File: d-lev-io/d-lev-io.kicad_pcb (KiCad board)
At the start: 2 copper layers, 92 parts, among them J1 USB_C_Receptacle_USB2.0, J2 PJ-059A, J3 Conn_01x12_MountingPin, J4 MIDI_OUT_JACK, J5 PROG_HDR, SW1 SW_Push, SW2 SW_Push, SW3 SW_Push, U1 ATSAMD11D14A-M, U2 TPS54202DDC, U4 MIC5219-3.3YM5, U6 74AHC1G126

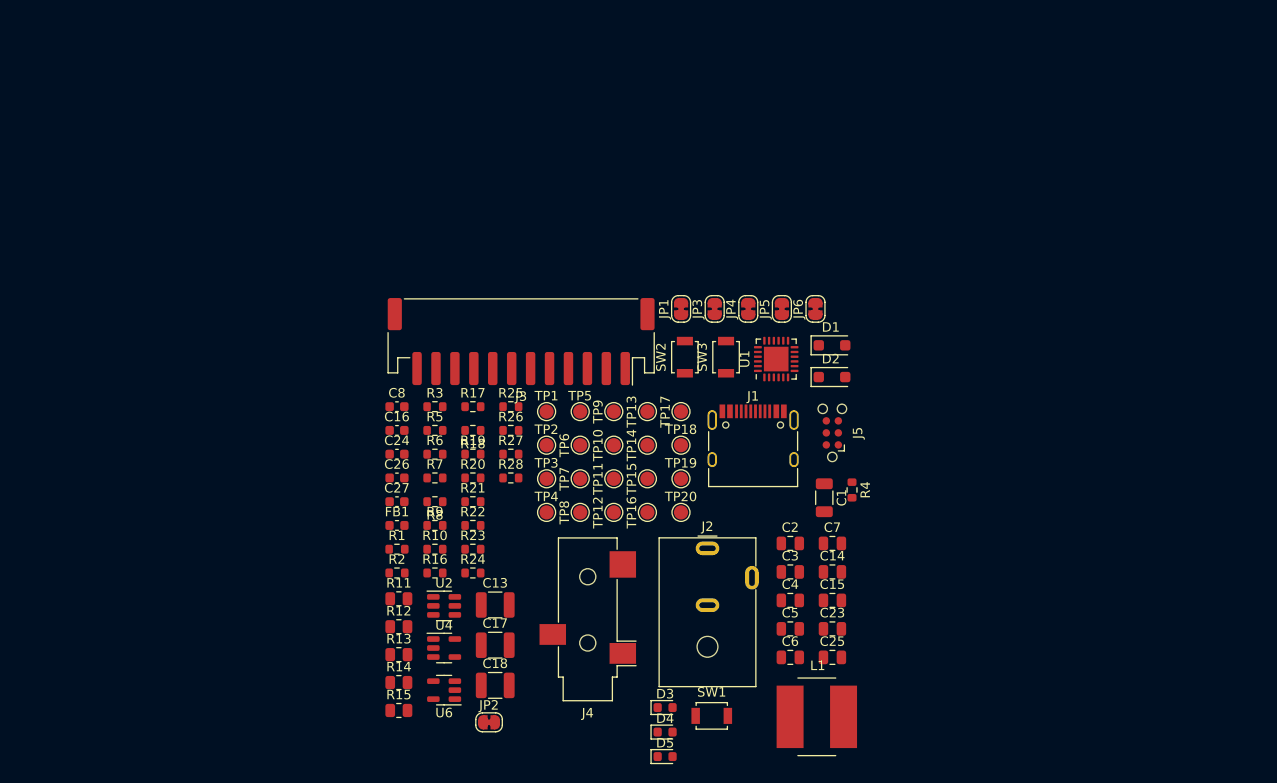
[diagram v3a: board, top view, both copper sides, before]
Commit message: Added DAC schematic to I/O board
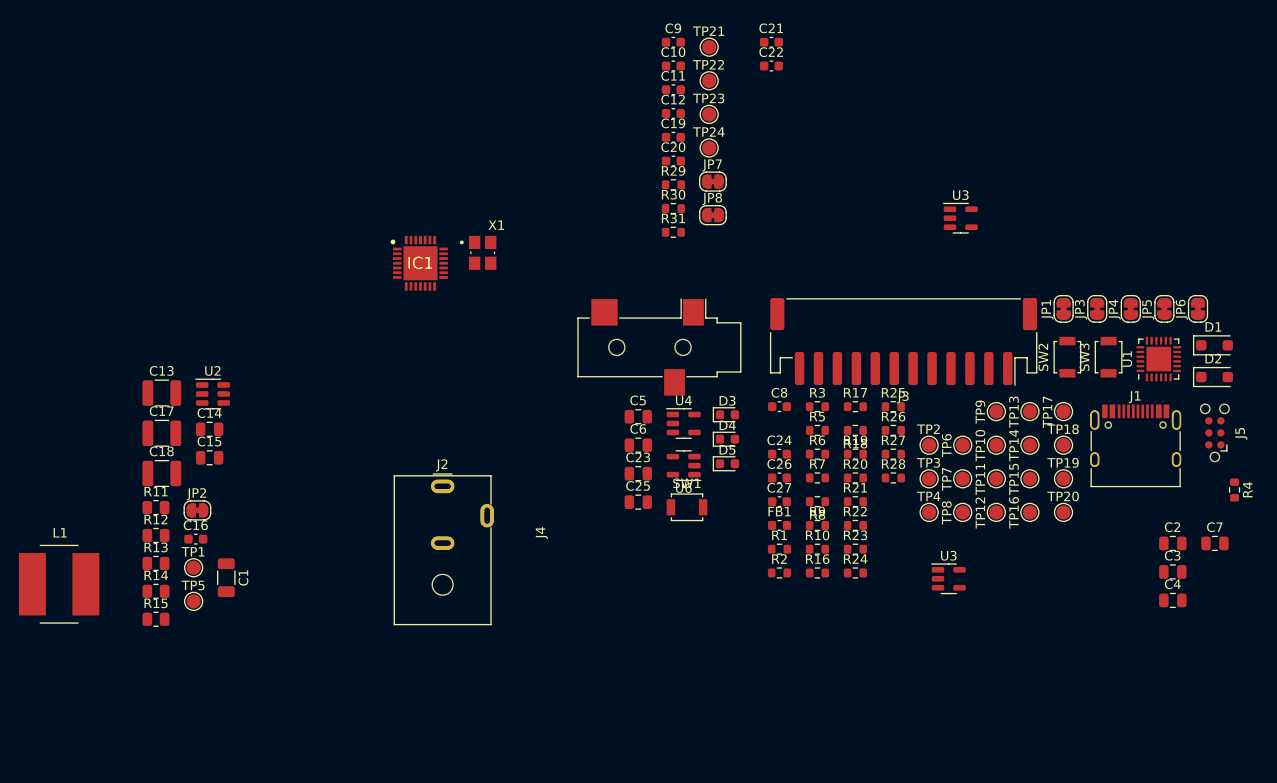
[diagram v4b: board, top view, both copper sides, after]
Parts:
- added C10: 33p, Capacitor_SMD:C_0603_1608Metric, F.Cu at (120.9, 64.2)
- added C11: 1u, Capacitor_SMD:C_0603_1608Metric, F.Cu at (120.9, 66.8)
- added C12: 4.7u, Capacitor_SMD:C_0603_1608Metric, F.Cu at (120.9, 69.3)
- added C19: 1u, Capacitor_SMD:C_0603_1608Metric, F.Cu at (120.9, 71.8)
- added C20: 1u, Capacitor_SMD:C_0603_1608Metric, F.Cu at (120.9, 74.3)
- added C21: 1u, Capacitor_SMD:C_0603_1608Metric, F.Cu at (131.3, 61.7)
- added C22: 1u, Capacitor_SMD:C_0603_1608Metric, F.Cu at (131.3, 64.2)
- added C9: 33p, Capacitor_SMD:C_0603_1608Metric, F.Cu at (120.9, 61.7)
- added IC1: ES9010K2M, ess-dac:QFN50P500X500X90-29N-D, F.Cu at (94.2, 85.1)
- added JP7: ADDRSEL, Jumper:SolderJumper-2_P1.3mm_Bridged_RoundedPad1.0x1.5mm, F.Cu at (125.1, 76.5)
- added JP8: NET_TIE, Jumper:SolderJumper-2_P1.3mm_Bridged_RoundedPad1.0x1.5mm, F.Cu at (125.1, 80.0)
- added R29: 56k, Resistor_SMD:R_0603_1608Metric, F.Cu at (120.9, 76.8)
- added R30: 20, Resistor_SMD:R_0603_1608Metric, F.Cu at (120.9, 79.3)
- added R31: 499k, Resistor_SMD:R_0603_1608Metric, F.Cu at (120.9, 81.8)
- added TP21: VREG, TestPoint:TestPoint_Pad_D1.5mm, F.Cu at (124.7, 62.3)
- added TP22: VREF, TestPoint:TestPoint_Pad_D1.5mm, F.Cu at (124.7, 65.8)
- added TP23: VCCA, TestPoint:TestPoint_Pad_D1.5mm, F.Cu at (124.7, 69.4)
- added TP24: DVDD, TestPoint:TestPoint_Pad_D1.5mm, F.Cu at (124.7, 72.9)
- added U3: ADP151-3.3, Package_TO_SOT_SMD:TSOT-23-5, F.Cu at (150.0, 118.4)
- added U3: ADP151-3.3, Package_TO_SOT_SMD:TSOT-23-5, F.Cu at (151.3, 80.3)
- added X1: 7M-50.000MAAJ-T, ess-dac:XTAL_7M-50.000MAAJ-T, F.Cu at (100.8, 84.0)
- moved L1 81.3 mm to (56.0, 119.0)
- moved C14 67.5 mm to (71.9, 102.6)
- moved C15 67.5 mm to (71.9, 105.6)
- moved C1 63.7 mm to (73.7, 118.3)
- moved TP5 45.5 mm to (70.2, 120.8)
- moved C13 41.7 mm to (66.8, 98.8)
- moved C17 41.7 mm to (66.8, 103.1)
- moved C18 41.7 mm to (66.8, 107.3)
- moved TP1 40.8 mm to (70.2, 117.3)
- moved C24 40.4 mm to (132.1, 105.3)
- moved C26 40.4 mm to (132.1, 107.8)
- moved C27 40.4 mm to (132.1, 110.3)
- moved C7 40.4 mm to (178.1, 114.7)
- moved C8 40.4 mm to (132.1, 100.2)
- moved FB1 40.4 mm to (132.1, 112.8)
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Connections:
- net /SAMD11/SCL renamed /DAC/SCL
- net /SAMD11/SDA renamed /DAC/SDA
- R3 pad 1: /USB.DM -> /SAMD11/USB.DM
- R4 pad 1: /USB.DP -> /SAMD11/USB.DP

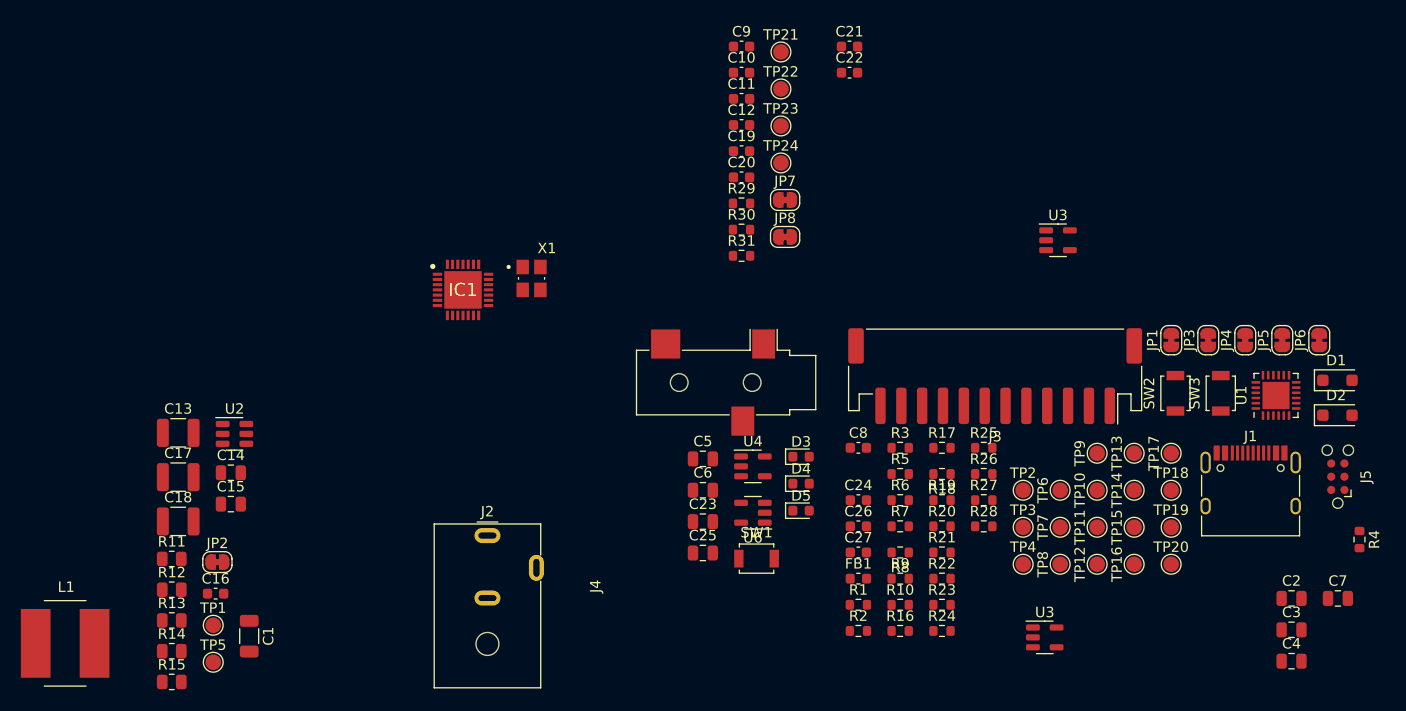
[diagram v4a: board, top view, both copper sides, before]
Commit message: add headphone amp
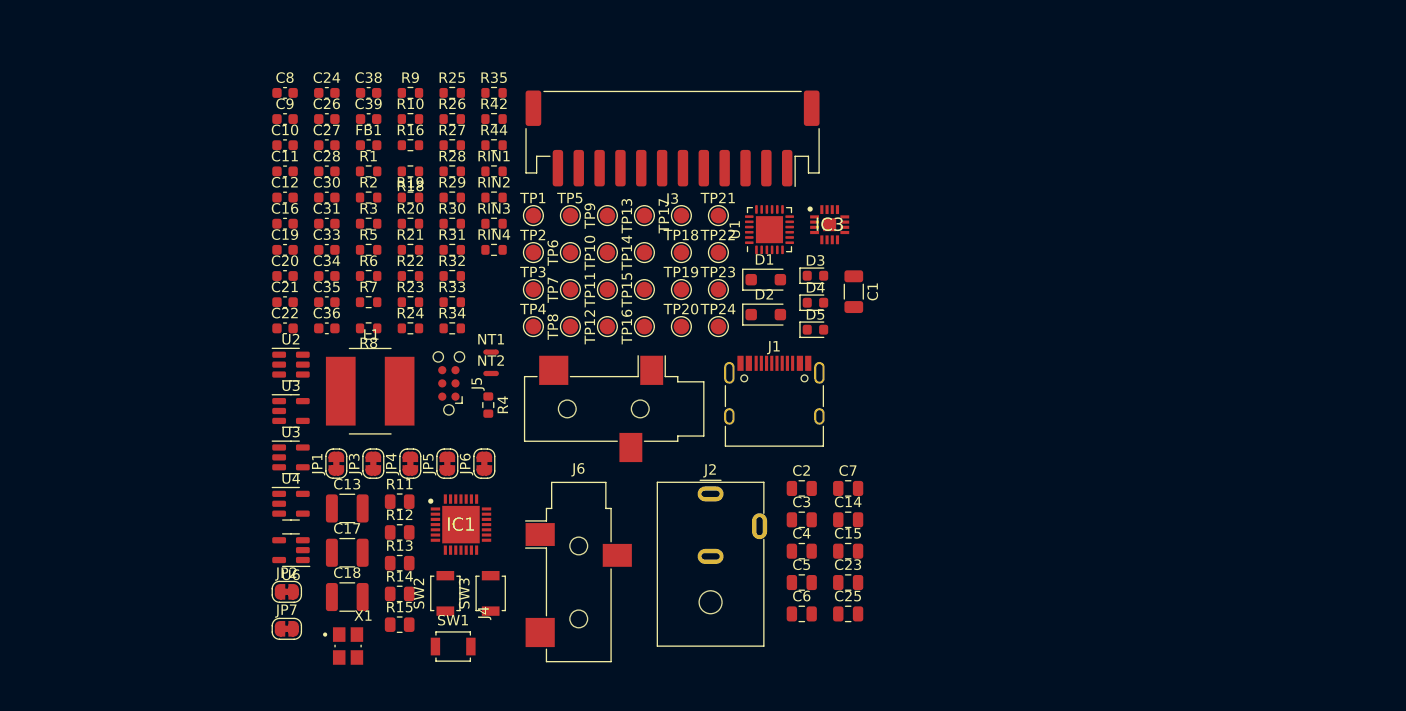
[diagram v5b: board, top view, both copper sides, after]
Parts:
- removed JP8: NET_TIE, Jumper:SolderJumper-2_P1.3mm_Bridged_RoundedPad1.0x1.5mm
- removed R17: 4.7k, Resistor_SMD:R_0603_1608Metric
- added C28: .47u, Capacitor_SMD:C_0603_1608Metric, F.Cu at (81.1, 73.7)
- added C30: .47u, Capacitor_SMD:C_0603_1608Metric, F.Cu at (81.1, 76.2)
- added C31: 1u, Capacitor_SMD:C_0603_1608Metric, F.Cu at (81.1, 78.7)
- added C33: .47u, Capacitor_SMD:C_0603_1608Metric, F.Cu at (81.1, 81.2)
- added C34: .47u, Capacitor_SMD:C_0603_1608Metric, F.Cu at (81.1, 83.8)
- added C35: 1u, Capacitor_SMD:C_0603_1608Metric, F.Cu at (81.1, 86.3)
- added C36: 1u, Capacitor_SMD:C_0603_1608Metric, F.Cu at (81.1, 88.8)
- added C38: 0.1u, Capacitor_SMD:C_0603_1608Metric, F.Cu at (85.1, 66.2)
- added C39: 1u, Capacitor_SMD:C_0603_1608Metric, F.Cu at (85.1, 68.7)
- added IC3: MAX97220AETE+T, theremin:QFN50P300X300X80-17N, F.Cu at (129.4, 78.8)
- added J6: MIDI_OUT_JACK, Connector_Audio:Jack_3.5mm_CUI_SJ-3523-SMT_Horizontal, F.Cu at (105.3, 112.2)
- added NT1: NetTie_2, NetTie:NetTie-2_SMD_Pad0.5mm, F.Cu at (96.9, 91.1)
- added NT2: NetTie_2, NetTie:NetTie-2_SMD_Pad0.5mm, F.Cu at (96.9, 93.1)
- added R32: 100, Resistor_SMD:R_0603_1608Metric, F.Cu at (93.1, 83.8)
- added R33: 100, Resistor_SMD:R_0603_1608Metric, F.Cu at (93.1, 86.3)
- added R34: 100, Resistor_SMD:R_0603_1608Metric, F.Cu at (93.1, 88.8)
- added R35: 0, Resistor_SMD:R_0603_1608Metric, F.Cu at (97.2, 66.2)
- added R42: 0, Resistor_SMD:R_0603_1608Metric, F.Cu at (97.2, 68.7)
- added R44: 0, Resistor_SMD:R_0603_1608Metric, F.Cu at (97.2, 71.2)
- added RIN1: 10k, Resistor_SMD:R_0603_1608Metric, F.Cu at (97.2, 73.7)
- added RIN2: 10k, Resistor_SMD:R_0603_1608Metric, F.Cu at (97.2, 76.2)
- added RIN3: 10k, Resistor_SMD:R_0603_1608Metric, F.Cu at (97.2, 78.7)
- added RIN4: 10k, Resistor_SMD:R_0603_1608Metric, F.Cu at (97.2, 81.2)
- R19: value 4.7k -> 100k
- U3 (x2): footprint Package_TO_SOT_SMD:TSOT-23-5 -> Package_TO_SOT_SMD:SOT-23-5
- moved J5 85.8 mm to (92.8, 94.1)
- moved R4 84.6 mm to (96.6, 96.1)
- moved JP3 81.0 mm to (85.6, 101.8)
- moved JP6 81.0 mm to (96.2, 101.8)
- moved JP1 81.0 mm to (82.0, 101.8)
- moved JP5 81.0 mm to (92.7, 101.8)
- moved JP4 81.0 mm to (89.1, 101.8)
- moved U3 75.4 mm to (77.7, 96.7)
- moved U3 74.4 mm to (77.7, 101.2)
- moved SW2 72.6 mm to (92.5, 114.2)
- moved SW3 72.6 mm to (96.8, 114.2)
- moved C1 66.8 mm to (131.7, 85.3)
- moved R10 66.2 mm to (89.1, 68.7)
- moved R16 66.2 mm to (89.1, 71.2)
- moved R9 66.2 mm to (89.1, 66.2)
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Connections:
- IC1 pad 24: /DAC/DAC.RESET -> /DAC/DAC.GPIO
- J3 pad 1: midi_to_fpga_3v -> Net-(J3-Pin_1)
- J3 pad 3: midi_from_fpga_3v -> Net-(J3-Pin_3)
- J3 pad 5: uart_tx_3v -> Net-(J3-Pin_5)
- J3 pad 7: uart_rx_3v -> Net-(J3-Pin_7)
- R19 pad 1: Net-(U1-PA15) -> /DAC/HPA_SHDN
- R19 pad 2: midi_from_fpga_3v -> +3.3VA
- TP11 pad 1: uart_rx_3v -> Net-(J3-Pin_7)
- TP13 pad 1: uart_tx_3v -> Net-(J3-Pin_5)
- TP15 pad 1: midi_from_fpga_3v -> Net-(J3-Pin_3)
- TP17 pad 1: midi_to_fpga_3v -> Net-(J3-Pin_1)
- U1 pad 11: Net-(U1-PA14) -> midi_to_fpga_3v
- U1 pad 12: Net-(U1-PA15) -> midi_from_fpga_3v
- U1 pad 25: (no net) -> GND

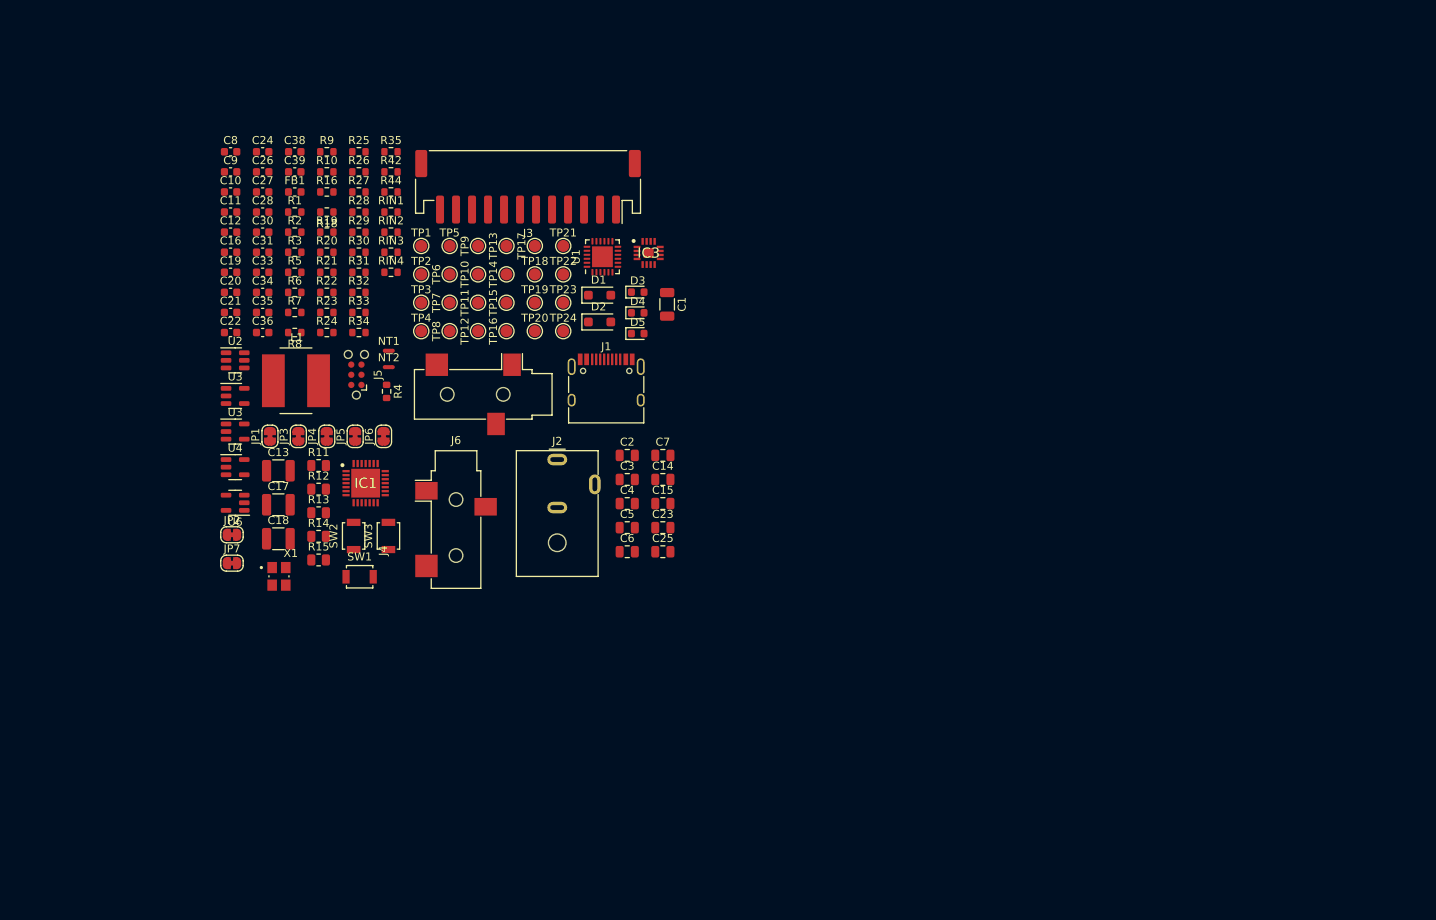
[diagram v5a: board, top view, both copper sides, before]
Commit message: io board more analog schematic capture
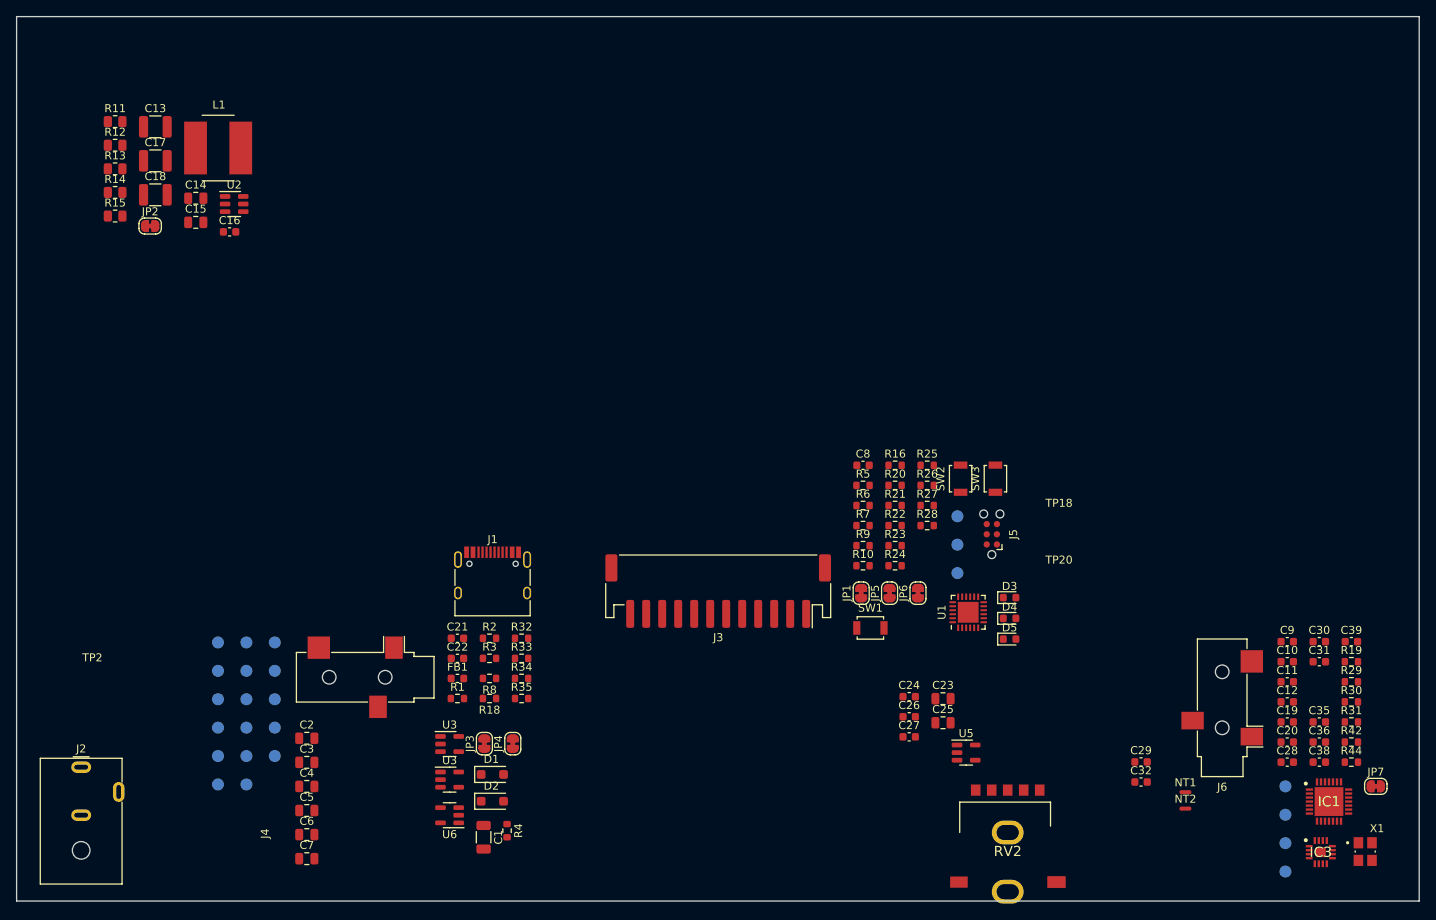
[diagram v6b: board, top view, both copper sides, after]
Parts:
- removed C33, C34: .47u, Capacitor_SMD:C_0603_1608Metric
- removed RIN1, RIN2, RIN3, RIN4: 10k, Resistor_SMD:R_0603_1608Metric
- removed U4: MIC5219-3.3YM5, Package_TO_SOT_SMD:SOT-23-5
- added C29: .47u, Capacitor_SMD:C_0603_1608Metric, F.Cu at (190.9, 142.5)
- added C32: .47u, Capacitor_SMD:C_0603_1608Metric, F.Cu at (190.9, 145.0)
- added RV2: 20K, theremin:RK10J12R0A0B, F.Cu at (174.2, 155.0)
- added U5: AP2112K-3.3, Package_TO_SOT_SMD:SOT-23-5, F.Cu at (169.0, 141.3)
- J6: value MIDI_OUT_JACK -> HEADPHONE
- TP1, TP10, TP11, TP12, TP13, TP14, TP15, TP16, TP17, TP18, TP19, TP2, TP20, TP21, TP22, TP23, TP24, TP3, TP4, TP5, TP6, TP7, TP8, TP9: moved to B.Cu
- moved C38 149.1 mm to (213.2, 142.5)
- moved JP7 145.7 mm to (220.2, 145.5)
- moved C28 145.4 mm to (209.2, 142.5)
- moved C10 144.5 mm to (209.2, 129.9)
- moved C11 144.5 mm to (209.2, 132.4)
- moved C12 144.5 mm to (209.2, 134.9)
- moved C9 144.5 mm to (209.2, 127.4)
- moved C39 144.5 mm to (217.2, 127.4)
- moved C19 143.5 mm to (209.2, 137.5)
- moved C20 143.5 mm to (209.2, 140.0)
- moved C30 141.7 mm to (213.2, 127.4)
- moved C31 141.7 mm to (213.2, 129.9)
- moved C35 141.7 mm to (213.2, 137.5)
- moved C36 141.7 mm to (213.2, 140.0)
- moved X1 140.1 mm to (218.9, 153.7)
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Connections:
- net /DAC/AMP_SGND renamed /DAC/OUT_SE.G
- C24 pad 2: +5V -> +3V3
- C26 pad 2: +3V3 -> +5V
- R19 pad 2: +3.3VA -> /DAC/AMP_PVDD
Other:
- board outline added: 175.3 x 110.6 mm
